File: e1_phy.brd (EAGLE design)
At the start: 100 x 75 mm, 125 parts, among them IC2 LD117AS33TR, IC3 LD117AS33TR, IC4 MCP4725, U1 IDT82V2081, U2 GPS_GNS_2201, U3 VCTCXO-CONNORWINFIELD, U4 VCXO_TAITIEN_VT, U5 IP4234CZ6, X2 SMA-142-0701-801/806, X3 JACK2.5_SJ-2523, X4 0446200002

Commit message: Implement review comment: R1 120 Ohms, R2, R2 9 Ohs
Termination on Rx input and output impedance on Tx.
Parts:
- R1: value DNP -> 120R
- R2, R8: value DNP -> 9R
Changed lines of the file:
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@@
 </element>
 <element name="TR1" library="laforge" package="PULSE_BH" value="PULSE_T1094NL" x="31.59125" y="12.7" rot="R180"/>
-<element name="R1" library="rcl" package="R0603" value="DNP" x="39.37" y="10.00125" smashed="yes" rot="R90">
+<element name="R1" library="rcl" package="R0603" value="120R" x="39.37" y="10.00125" smashed="yes" rot="R90">
 <attribute name="NAME" x="38.89375" y="7.46125" size="0.6096" layer="25" font="vector"/>
 <attribute name="VALUE" x="41.275" y="9.36625" size="1.27" layer="27" rot="R90"/>
 </element>
-<element name="R2" library="rcl" package="R0603" value="DNP" x="39.37" y="13.97" smashed="yes" rot="R180">
+<element name="R2" library="rcl" package="R0603" value="9R" x="39.37" y="13.97" smashed="yes" rot="R180">
 <attribute name="NAME" x="39.21125" y="18.0975" size="0.6096" layer="25" font="vector"/>
 <attribute name="VALUE" x="40.005" y="15.875" size="1.27" layer="27" rot="R180"/>
 </element>
-<element name="R8" library="rcl" package="R0603" value="DNP" x="39.37" y="16.51" smashed="yes" rot="R180">
+<element name="R8" library="rcl" package="R0603" value="9R" x="39.37" y="16.51" smashed="yes" rot="R180">
 <attribute name="NAME" x="39.21125" y="19.84375" size="0.6096" layer="25" font="vector"/>
 <attribute name="VALUE" x="40.005" y="18.415" size="1.27" layer="27" rot="R180"/>

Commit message: Implement review comment: LIU move signal from LOS to #INT
 - LIU move signal from LOS to #INT
   -> Interrupt can be generated on LOS anyway.
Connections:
- removed net LOS_LIU: U$1.32, U1.7
- new net #LIU_INT: U$1.32, U1.20
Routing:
- net #LIU_INT: track 0.00 -> 75.5 mm, vias 0 -> 2
- net LOS_LIU: track 67.3 -> 0.00 mm, vias 2 -> 0
- net GND: vias 96 -> 99
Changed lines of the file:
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@@
 <wire x1="36.35375" y1="20.79625" x2="36.67125" y2="20.47875" width="0.1524" layer="1" curve="-90"/>
 <contactref element="U5" pad="2"/>
+<via x="66.83375" y="14.605" extent="1-16" drill="0.35"/>
+<via x="68.73875" y="12.065" extent="1-16" drill="0.35"/>
+<via x="65.405" y="14.605" extent="1-16" drill="0.35"/>
 </signal>
 <signal name="LINE_PIN1">
@@
 <wire x1="60.77" y1="11.88923125" x2="60.83176875" y2="11.951" width="0.1524" layer="1"/>
 </signal>
-<signal name="LOS_LIU">
-<contactref element="U$1" pad="32"/>
-<wire x1="34.1647375" y1="40.3376" x2="38.57625" y2="40.3376" width="0.1524" layer="1"/>
-<wire x1="33.2038" y1="41.2985375" x2="33.2038" y2="43.78495" width="0.1524" layer="1"/>
-<wire x1="33.2038" y1="41.2985375" x2="34.1647375" y2="40.3376" width="0.1524" layer="1"/>
-<wire x1="38.57625" y1="40.3376" x2="39.07385" y2="39.84" width="0.1524" layer="1"/>
-<wire x1="39.07385" y1="39.84" x2="39.37" y2="39.84" width="0.1524" layer="1"/>
-<via x="39.37" y="39.84" extent="1-16" drill="0.35"/>
-<wire x1="39.37" y1="39.84" x2="39.9010875" y2="39.84" width="0.1524" layer="16"/>
-<wire x1="39.9010875" y1="39.84" x2="40.3559875" y2="39.3851" width="0.1524" layer="16"/>
-<wire x1="40.3559875" y1="39.3851" x2="41.4672375" y2="39.3851" width="0.1524" layer="16"/>
-<wire x1="41.4672375" y1="39.3851" x2="42.2573375" y2="38.595" width="0.1524" layer="16"/>
-<wire x1="33.2038" y1="43.78495" x2="33.08" y2="43.90875" width="0.1524" layer="1"/>
-<wire x1="33.08" y1="43.90875" x2="33.08" y2="45.02" width="0.1524" layer="1"/>
-<contactref element="U1" pad="7"/>
-<wire x1="42.545" y1="10.795" x2="42.2573375" y2="11.0826625" width="0.1524" layer="16"/>
-<wire x1="42.2573375" y1="38.595" x2="42.2573375" y2="11.0826625" width="0.1524" layer="16"/>
-<wire x1="65.57" y1="8.17" x2="65.57" y2="10.47125" width="0.1524" layer="1"/>
-<wire x1="65.57" y1="10.47125" x2="65.56375" y2="10.4775" width="0.1524" layer="1"/>
-<via x="65.56375" y="10.4775" extent="1-16" drill="0.35"/>
-<wire x1="65.56375" y1="10.4775" x2="65.24625" y2="10.795" width="0.1524" layer="16"/>
-<wire x1="65.24625" y1="10.795" x2="42.545" y2="10.795" width="0.1524" layer="16"/>
-</signal>
 <signal name="#RST_LIU">
 <contactref element="U$1" pad="31"/>
@@
 <wire x1="10.325" y1="50.33" x2="10.65" y2="50.655" width="0.1524" layer="1"/>
 </signal>
+<signal name="#LIU_INT">
+<contactref element="U1" pad="20"/>
+<contactref element="U$1" pad="32"/>
+<wire x1="34.1647375" y1="40.3376" x2="38.57625" y2="40.3376" width="0.1524" layer="1"/>
+<wire x1="33.2038" y1="41.2985375" x2="33.2038" y2="43.78495" width="0.1524" layer="1"/>
+<wire x1="33.2038" y1="41.2985375" x2="34.1647375" y2="40.3376" width="0.1524" layer="1"/>
+<wire x1="38.57625" y1="40.3376" x2="39.07385" y2="39.84" width="0.1524" layer="1"/>
+<wire x1="39.07385" y1="39.84" x2="39.37" y2="39.84" width="0.1524" layer="1"/>
+<via x="39.37" y="39.84" extent="1-16" drill="0.35"/>
+<wire x1="39.37" y1="39.84" x2="39.9010875" y2="39.84" width="0.1524" layer="16"/>
+<wire x1="39.9010875" y1="39.84" x2="40.3559875" y2="39.3851" width="0.1524" layer="16"/>
+<wire x1="40.3559875" y1="39.3851" x2="41.4672375" y2="39.3851" width="0.1524" layer="16"/>
+<wire x1="41.4672375" y1="39.3851" x2="42.2573375" y2="38.595" width="0.1524" layer="16"/>
+<wire x1="33.2038" y1="43.78495" x2="33.08" y2="43.90875" width="0.1524" layer="1"/>
+<wire x1="33.08" y1="43.90875" x2="33.08" y2="45.02" width="0.1524" layer="1"/>
+<wire x1="42.545" y1="10.795" x2="42.2573375" y2="11.0826625" width="0.1524" layer="16"/>
+<wire x1="42.2573375" y1="38.595" x2="42.2573375" y2="11.0826625" width="0.1524" layer="16"/>
+<wire x1="65.57" y1="10.47125" x2="65.56375" y2="10.4775" width="0.1524" layer="1"/>
+<via x="65.56375" y="10.4775" extent="1-16" drill="0.35"/>
+<wire x1="65.56375" y1="10.4775" x2="65.24625" y2="10.795" width="0.1524" layer="16"/>
+<wire x1="65.24625" y1="10.795" x2="42.545" y2="10.795" width="0.1524" layer="16"/>
+<wire x1="70.57" y1="16.37" x2="66.37625" y2="16.37" width="0.1524" layer="1"/>
+<wire x1="66.37625" y1="16.37" x2="66.19875" y2="16.1925" width="0.1524" layer="1"/>
+<wire x1="66.19875" y1="16.1925" x2="66.19875" y2="11.1" width="0.1524" layer="1"/>
+<wire x1="66.19875" y1="11.1" x2="65.57" y2="10.47125" width="0.1524" layer="1"/>
+</signal>
 </signals>

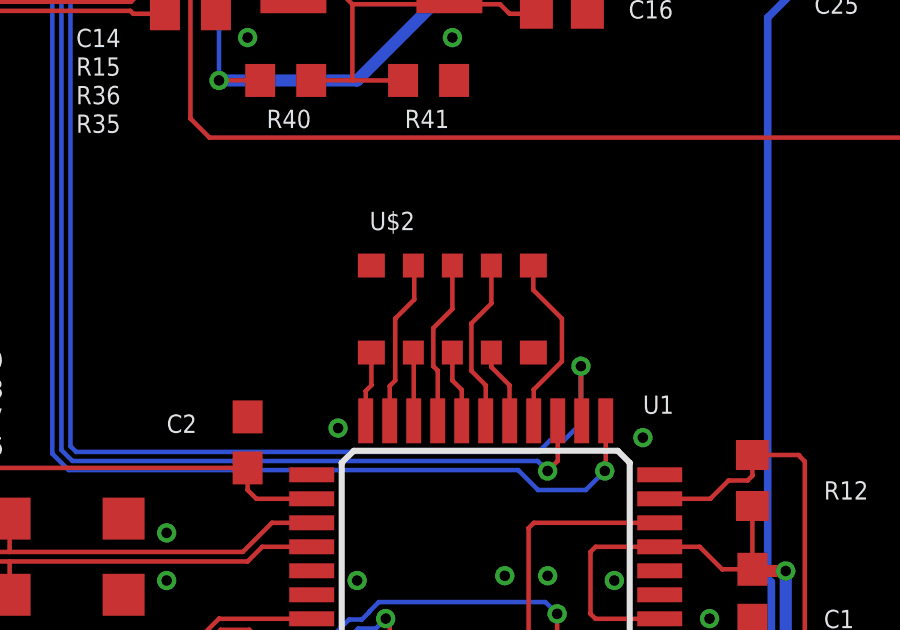
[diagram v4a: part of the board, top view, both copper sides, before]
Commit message: Implementation of review comment:
   Removed octal resistor array, introduced quad resistor array,
   will be used for various pullups.
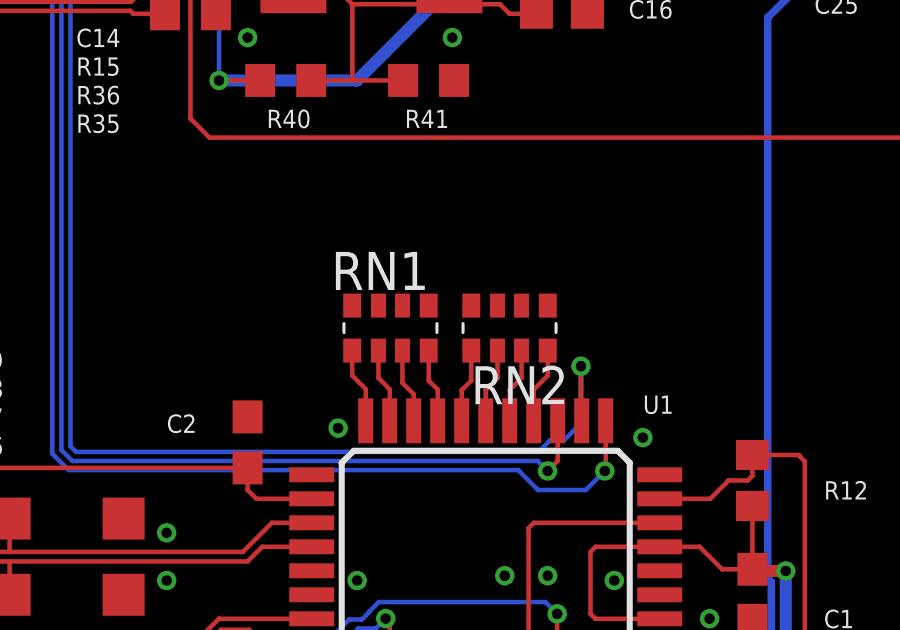
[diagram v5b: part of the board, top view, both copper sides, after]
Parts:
- removed U$2: MNR 8x10k, laforge:MNR35
- added RN1, RN2: (no value), resistor-dil:EXB38V
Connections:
- net AD0: now also RN2.8; no longer U$2.6
- net AD1: now also RN2.7; no longer U$2.4
- net AD2: now also RN2.6; no longer U$2.7
- net AD3: now also RN2.5; no longer U$2.3
- net AD4: now also RN1.4; no longer U$2.8
- net AD5: now also RN1.3; no longer U$2.2
- net AD6: now also RN1.2; no longer U$2.9
- net AD7: now also RN1.1; no longer U$2.1
- net GND: now also RN1.5, RN1.6, RN1.7, RN1.8, RN2.1, RN2.2, RN2.3, RN2.4; no longer U$2.10, U$2.5
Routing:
- net AD0: track 5.96 -> 2.53 mm
- net AD2: track 5.65 -> 2.50 mm
- net AD4: track 5.50 -> 2.46 mm
- net AD6: track 5.53 -> 2.50 mm
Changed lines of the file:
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@@
 <attribute name="VALUE" x="73.5251" y="9.525" size="1.778" layer="27" rot="R90"/>
-</element>
-<element name="U$2" library="laforge" package="MNR35" value="MNR 8x10k" x="63.65875" y="23.495" smashed="yes">
-<attribute name="NAME" x="60.9" y="26.125" size="0.6096" layer="25" font="vector"/>
-<attribute name="VALUE" x="58.45875" y="19.595" size="1.27" layer="27"/>
 </element>
 <element name="TR1" library="laforge" package="PULSE_BH" value="PULSE_T1094NL" x="31.59125" y="12.7" rot="R180"/>
@@
 <element name="U5" library="laforge" package="TSOP-6" value="IP4234CZ6" x="12.7" y="49.53">
 <attribute name="OC_DIGIKEY" value="568-5869-1-ND" x="12.7" y="49.53" size="1.778" layer="27" display="off"/>
+</element>
+<element name="RN1" library="resistor-dil" library_urn="urn:adsk.eagle:library:342" package="EXB38V" package3d_urn="urn:adsk.eagle:package:24923/1" value="" x="61.595" y="22.86">
+<attribute name="MF" value="" x="61.595" y="22.86" size="1.778" layer="27" display="off"/>
+<attribute name="MPN" value="" x="61.595" y="22.86" size="1.778" layer="27" display="off"/>
+<attribute name="OC_FARNELL" value="unknown" x="61.595" y="22.86" size="1.778" layer="27" display="off"/>
+<attribute name="OC_NEWARK" value="unknown" x="61.595" y="22.86" size="1.778" layer="27" display="off"/>
+</element>
+<element name="RN2" library="resistor-dil" library_urn="urn:adsk.eagle:library:342" package="EXB38V" package3d_urn="urn:adsk.eagle:package:24923/1" value="" x="65.56375" y="22.86" rot="R180">
+<attribute name="MF" value="" x="65.56375" y="22.86" size="1.778" layer="27" rot="R180" display="off"/>
+<attribute name="MPN" value="" x="65.56375" y="22.86" size="1.778" layer="27" rot="R180" display="off"/>
+<attribute name="OC_FARNELL" value="unknown" x="65.56375" y="22.86" size="1.778" layer="27" rot="R180" display="off"/>
+<attribute name="OC_NEWARK" value="unknown" x="65.56375" y="22.86" size="1.778" layer="27" rot="R180" display="off"/>
 </element>
 </elements>
@@
 <contactref element="U1" pad="14"/>
 <contactref element="U1" pad="13"/>
-<contactref element="U$2" pad="5"/>
-<contactref element="U$2" pad="10"/>
 <contactref element="R9" pad="2"/>
 <contactref element="C1" pad="2"/>
@@
 <via x="68.73875" y="12.065" extent="1-16" drill="0.35"/>
 <via x="65.405" y="14.605" extent="1-16" drill="0.35"/>
+<contactref element="RN1" pad="5"/>
+<contactref element="RN2" pad="1"/>
+<contactref element="RN1" pad="6"/>
+<contactref element="RN1" pad="7"/>
+<contactref element="RN2" pad="2"/>
+<contactref element="RN2" pad="3"/>
+<contactref element="RN2" pad="4"/>
+<contactref element="RN1" pad="8"/>
 </signal>
 <signal name="LINE_PIN1">
@@
 <signal name="AD0">
 <contactref element="U1" pad="26"/>
-<contactref element="U$2" pad="6"/>
-<wire x1="66.37" y1="19.77" x2="66.37" y2="20.80875" width="0.1524" layer="1"/>
-<wire x1="66.37" y1="20.80875" x2="67.31" y2="21.74875" width="0.1524" layer="1"/>
-<wire x1="67.31" y1="21.74875" x2="67.31" y2="23.1775" width="0.1524" layer="1"/>
-<wire x1="67.31" y1="23.1775" x2="66.3575" y2="24.13" width="0.1524" layer="1"/>
-<wire x1="66.3575" y1="24.13" x2="66.3575" y2="24.94375" width="0.1524" layer="1"/>
-<wire x1="66.3575" y1="24.94375" x2="66.35875" y2="24.945" width="0.1524" layer="1"/>
+<contactref element="RN2" pad="8"/>
+<wire x1="66.37" y1="20.80875" x2="66.37" y2="19.77" width="0.1524" layer="1"/>
+<wire x1="66.83875" y1="22.11" x2="66.83875" y2="21.2775" width="0.1524" layer="1"/>
+<wire x1="66.83875" y1="21.2775" x2="66.37" y2="20.80875" width="0.1524" layer="1"/>
 </signal>
 <signal name="AD1">
 <contactref element="U1" pad="27"/>
-<contactref element="U$2" pad="4"/>
-<wire x1="65.57" y1="19.77" x2="65.56375" y2="19.77625" width="0.1524" layer="1"/>
-<wire x1="65.56375" y1="19.77625" x2="65.56375" y2="20.955" width="0.1524" layer="1"/>
-<wire x1="65.56375" y1="20.955" x2="64.95875" y2="21.56" width="0.1524" layer="1"/>
-<wire x1="64.95875" y1="21.56" x2="64.95875" y2="22.045" width="0.1524" layer="1"/>
+<contactref element="RN2" pad="7"/>
+<wire x1="65.57" y1="20.8025" x2="65.57" y2="19.77" width="0.1524" layer="1"/>
+<wire x1="65.96375" y1="22.11" x2="65.96375" y2="21.19625" width="0.1524" layer="1"/>
+<wire x1="65.96375" y1="21.19625" x2="65.57" y2="20.8025" width="0.1524" layer="1"/>
 </signal>
 <signal name="AD4">
 <contactref element="U1" pad="30"/>
-<contactref element="U$2" pad="8"/>
-<wire x1="63.17" y1="19.77" x2="63.17" y2="21.44375" width="0.1524" layer="1"/>
-<wire x1="63.17" y1="21.44375" x2="63.02375" y2="21.59" width="0.1524" layer="1"/>
-<wire x1="63.02375" y1="21.59" x2="63.02375" y2="22.86" width="0.1524" layer="1"/>
-<wire x1="63.02375" y1="22.86" x2="63.65875" y2="23.495" width="0.1524" layer="1"/>
-<wire x1="63.65875" y1="23.495" x2="63.65875" y2="24.945" width="0.1524" layer="1"/>
+<contactref element="RN1" pad="4"/>
+<wire x1="63.17" y1="20.80875" x2="63.17" y2="19.77" width="0.1524" layer="1"/>
+<wire x1="62.87" y1="22.11" x2="62.87" y2="21.10875" width="0.1524" layer="1"/>
+<wire x1="62.87" y1="21.10875" x2="63.17" y2="20.80875" width="0.1524" layer="1"/>
 </signal>
 <signal name="AD3">
 <contactref element="U1" pad="29"/>
-<contactref element="U$2" pad="3"/>
-<wire x1="63.97" y1="19.77" x2="63.97" y2="20.8025" width="0.1524" layer="1"/>
-<wire x1="63.97" y1="20.8025" x2="63.65875" y2="21.11375" width="0.1524" layer="1"/>
-<wire x1="63.65875" y1="21.11375" x2="63.65875" y2="22.045" width="0.1524" layer="1"/>
+<contactref element="RN2" pad="5"/>
+<wire x1="63.97" y1="20.79" x2="63.97" y2="19.77" width="0.1524" layer="1"/>
+<wire x1="64.28875" y1="22.11" x2="64.28875" y2="21.10875" width="0.1524" layer="1"/>
+<wire x1="64.28875" y1="21.10875" x2="63.97" y2="20.79" width="0.1524" layer="1"/>
 </signal>
 <signal name="AD2">
 <contactref element="U1" pad="28"/>
-<contactref element="U$2" pad="7"/>
-<wire x1="64.77" y1="19.77" x2="64.77" y2="20.955" width="0.1524" layer="1"/>
-<wire x1="64.77" y1="20.955" x2="64.29375" y2="21.43125" width="0.1524" layer="1"/>
-<wire x1="64.29375" y1="21.43125" x2="64.29375" y2="23.01875" width="0.1524" layer="1"/>
-<wire x1="64.95875" y1="23.68375" x2="64.95875" y2="24.945" width="0.1524" layer="1"/>
-<wire x1="64.29375" y1="23.01875" x2="64.95875" y2="23.68375" width="0.1524" layer="1"/>
+<contactref element="RN2" pad="6"/>
+<wire x1="64.77" y1="20.79625" x2="64.77" y2="19.77" width="0.1524" layer="1"/>
+<wire x1="65.16375" y1="22.11" x2="65.16375" y2="21.19" width="0.1524" layer="1"/>
+<wire x1="65.16375" y1="21.19" x2="64.77" y2="20.79625" width="0.1524" layer="1"/>
 </signal>
 <signal name="AD5">
 <contactref element="U1" pad="31"/>
-<contactref element="U$2" pad="2"/>
-<wire x1="62.37" y1="19.77" x2="62.37" y2="22.03375" width="0.1524" layer="1"/>
-<wire x1="62.37" y1="22.03375" x2="62.35875" y2="22.045" width="0.1524" layer="1"/>
+<contactref element="RN1" pad="3"/>
+<wire x1="62.37" y1="20.65625" x2="62.37" y2="19.77" width="0.1524" layer="1"/>
+<wire x1="61.995" y1="22.11" x2="61.995" y2="21.03125" width="0.1524" layer="1"/>
+<wire x1="61.995" y1="21.03125" x2="62.37" y2="20.65625" width="0.1524" layer="1"/>
 </signal>
 <signal name="AD6">
 <contactref element="U1" pad="32"/>
-<contactref element="U$2" pad="9"/>
-<wire x1="61.57" y1="19.77" x2="61.57" y2="20.93" width="0.1524" layer="1"/>
-<wire x1="61.57" y1="20.93" x2="61.75375" y2="21.11375" width="0.1524" layer="1"/>
-<wire x1="61.75375" y1="21.11375" x2="61.75375" y2="23.1775" width="0.1524" layer="1"/>
-<wire x1="61.75375" y1="23.1775" x2="62.38875" y2="23.8125" width="0.1524" layer="1"/>
-<wire x1="62.38875" y1="23.8125" x2="62.38875" y2="24.915" width="0.1524" layer="1"/>
-<wire x1="62.38875" y1="24.915" x2="62.35875" y2="24.945" width="0.1524" layer="1"/>
+<contactref element="RN1" pad="2"/>
+<wire x1="61.57" y1="20.82125" x2="61.57" y2="19.77" width="0.1524" layer="1"/>
+<wire x1="61.195" y1="22.11" x2="61.195" y2="21.19625" width="0.1524" layer="1"/>
+<wire x1="61.195" y1="21.19625" x2="61.57" y2="20.82125" width="0.1524" layer="1"/>
 </signal>
 <signal name="AD7">
 <contactref element="U1" pad="33"/>
-<contactref element="U$2" pad="1"/>
-<wire x1="60.77" y1="19.77" x2="60.77" y2="20.765" width="0.1524" layer="1"/>
-<wire x1="60.77" y1="20.765" x2="60.96" y2="20.955" width="0.1524" layer="1"/>
-<wire x1="60.96" y1="20.955" x2="60.96" y2="22.04375" width="0.1524" layer="1"/>
-<wire x1="60.96" y1="22.04375" x2="60.95875" y2="22.045" width="0.1524" layer="1"/>
+<contactref element="RN1" pad="1"/>
+<wire x1="60.77" y1="20.8275" x2="60.77" y2="19.77" width="0.1524" layer="1"/>
+<wire x1="60.32" y1="22.11" x2="60.32" y2="21.2775" width="0.1524" layer="1"/>
+<wire x1="60.32" y1="21.2775" x2="60.77" y2="20.8275" width="0.1524" layer="1"/>
 </signal>
 <signal name="RTIP">
